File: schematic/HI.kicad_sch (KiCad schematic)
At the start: 5 parts, among them J2 USB_C_Receptacle_USB2.0, J4 Serial, SW1 Power Switch

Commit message: d
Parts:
- J2: footprint (none) -> 1KicadLib:USB4125-GF-A
- J4: footprint (none) -> Connector_PinHeader_2.54mm:PinHeader_1x03_P2.54mm_Vertical
- R8, R9: footprint (none) -> Resistor_SMD:R_0805_2012Metric_Pad1.20x1.40mm_HandSolder
- SW1: footprint (none) -> Connector_PinHeader_2.54mm:PinHeader_1x02_P2.54mm_Vertical
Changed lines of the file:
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@@
     (property "Reference" "J2" (id 0) (at 105.5878 30.0482 0))
     (property "Value" "USB_C_Receptacle_USB2.0" (id 1) (at 105.5878 32.3596 0))
-    (property "Footprint" "" (id 2) (at 106.68 52.07 0)
+    (property "Footprint" "1KicadLib:USB4125-GF-A" (id 2) (at 106.68 52.07 0)
       (effects (font (size 1.27 1.27)) hide)
     )
@@
       (effects (font (size 1.27 1.27)) (justify left))
     )
-    (property "Footprint" "" (id 2) (at 140.462 49.53 90)
+    (property "Footprint" "Resistor_SMD:R_0805_2012Metric_Pad1.20x1.40mm_HandSolder" (id 2) (at 140.462 49.53 90)
       (effects (font (size 1.27 1.27)) hide)
     )
@@
       (effects (font (size 1.27 1.27)) (justify left))
     )
-    (property "Footprint" "" (id 2) (at 148.082 46.99 90)
+    (property "Footprint" "Resistor_SMD:R_0805_2012Metric_Pad1.20x1.40mm_HandSolder" (id 2) (at 148.082 46.99 90)
       (effects (font (size 1.27 1.27)) hide)
     )
@@
     (property "Reference" "SW1" (id 0) (at 93.98 120.65 90))
     (property "Value" "Power Switch" (id 1) (at 91.44 124.46 90))
-    (property "Footprint" "" (id 2) (at 101.6 121.92 0)
+    (property "Footprint" "Connector_PinHeader_2.54mm:PinHeader_1x02_P2.54mm_Vertical" (id 2) (at 101.6 121.92 0)
       (effects (font (size 1.27 1.27)) hide)
     )
@@
       (effects (font (size 1.27 1.27)) (justify left))
     )
-    (property "Footprint" "" (id 2) (at 156.21 76.2 0)
+    (property "Footprint" "Connector_PinHeader_2.54mm:PinHeader_1x03_P2.54mm_Vertical" (id 2) (at 156.21 76.2 0)
       (effects (font (size 1.27 1.27)) hide)
     )

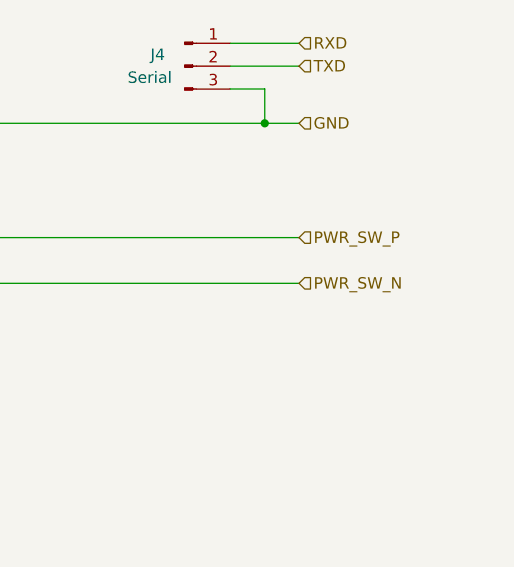
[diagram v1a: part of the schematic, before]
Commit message: beta boards routed
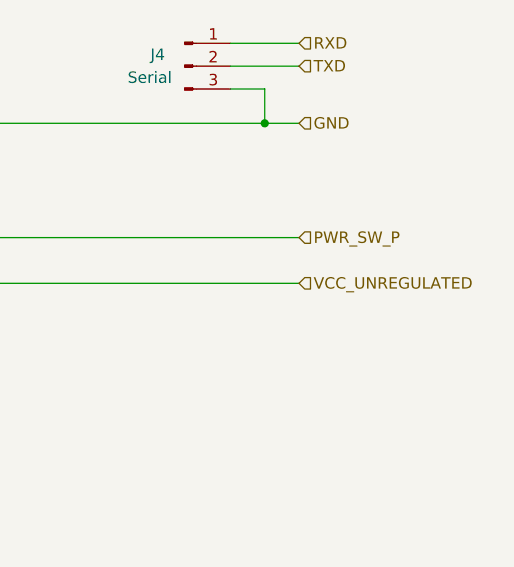
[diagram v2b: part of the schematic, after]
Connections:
- net PWR_SW_N renamed VCC_UNREGULATED
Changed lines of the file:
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@@
     (stroke (width 0) (type default) (color 0 0 0 0))
   )
-  (hierarchical_label "PWR_SW_N" (shape input) (at 168.91 100.33 0)
+  (hierarchical_label "VCC_UNREGULATED" (shape input) (at 168.91 100.33 0)
     (effects (font (size 1.27 1.27)) (justify left))
   )

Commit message: e
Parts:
- removed J4: Serial, Connector_PinHeader_2.54mm:PinHeader_1x03_P2.54mm_Vertical, symbol Connector:Conn_01x03_Male
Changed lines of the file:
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@@
   (junction (at 147.32 54.61) (diameter 0) (color 0 0 0 0)
   )
-  (junction (at 165.1 82.55) (diameter 0) (color 0 0 0 0)
-  )
   (junction (at 101.6 82.55) (diameter 0) (color 0 0 0 0)
-  )
-  (wire (pts (xy 101.6 82.55) (xy 165.1 82.55))
-    (stroke (width 0) (type default) (color 0 0 0 0))
   )
   (wire (pts (xy 101.6 114.3) (xy 101.6 107.95))
@@
   )
   (wire (pts (xy 147.32 54.61) (xy 147.32 55.88))
-    (stroke (width 0) (type default) (color 0 0 0 0))
-  )
-  (wire (pts (xy 161.29 78.74) (xy 165.1 78.74))
     (stroke (width 0) (type default) (color 0 0 0 0))
   )
@@
     (stroke (width 0) (type default) (color 0 0 0 0))
   )
-  (wire (pts (xy 168.91 66.04) (xy 163.83 66.04))
+  (wire (pts (xy 168.91 52.07) (xy 163.83 52.07))
     (stroke (width 0) (type default) (color 0 0 0 0))
   )
@@
     (stroke (width 0) (type default) (color 0 0 0 0))
   )
-  (wire (pts (xy 163.83 66.04) (xy 163.83 38.1))
+  (wire (pts (xy 163.83 52.07) (xy 163.83 38.1))
     (stroke (width 0) (type default) (color 0 0 0 0))
   )
-  (wire (pts (xy 165.1 82.55) (xy 168.91 82.55))
-    (stroke (width 0) (type default) (color 0 0 0 0))
-  )
-  (wire (pts (xy 161.29 73.66) (xy 168.91 73.66))
+  (wire (pts (xy 101.6 82.55) (xy 168.91 82.55))
     (stroke (width 0) (type default) (color 0 0 0 0))
   )
@@
     (stroke (width 0) (type default) (color 0 0 0 0))
   )
-  (wire (pts (xy 165.1 78.74) (xy 165.1 82.55))
-    (stroke (width 0) (type default) (color 0 0 0 0))
-  )
-  (wire (pts (xy 168.91 76.2) (xy 161.29 76.2))
-    (stroke (width 0) (type default) (color 0 0 0 0))
-  )
   (wire (pts (xy 93.98 82.55) (xy 93.98 76.2))
     (stroke (width 0) (type default) (color 0 0 0 0))
@@
     (effects (font (size 1.27 1.27)) (justify left))
   )
-  (hierarchical_label "RXD" (shape input) (at 168.91 73.66 0)
-    (effects (font (size 1.27 1.27)) (justify left))
-  )
   (hierarchical_label "PWR_SW_P" (shape input) (at 168.91 95.25 0)
     (effects (font (size 1.27 1.27)) (justify left))
   )
-  (hierarchical_label "VUSB" (shape input) (at 168.91 66.04 0)
+  (hierarchical_label "VUSB" (shape input) (at 168.91 52.07 0)
     (effects (font (size 1.27 1.27)) (justify left))
   )
   (hierarchical_label "GND" (shape input) (at 168.91 82.55 0)
-    (effects (font (size 1.27 1.27)) (justify left))
-  )
-  (hierarchical_label "TXD" (shape input) (at 168.91 76.2 0)
     (effects (font (size 1.27 1.27)) (justify left))
   )
@@
     (pin "2")
   )
-  (symbol (lib_id "Connector:Conn_01x03_Male") (at 156.21 76.2 0) (unit 1)
-    (in_bom yes) (on_board yes)
-    (property "Reference" "J4" (id 0) (at 152.4 74.93 0)
-      (effects (font (size 1.27 1.27)) (justify left))
-    )
-    (property "Value" "Serial" (id 1) (at 149.86 77.47 0)
-      (effects (font (size 1.27 1.27)) (justify left))
-    )
-    (property "Footprint" "Connector_PinHeader_2.54mm:PinHeader_1x03_P2.54mm_Vertical" (id 2) (at 156.21 76.2 0)
-      (effects (font (size 1.27 1.27)) hide)
-    )
-    (property "Datasheet" "~" (id 3) (at 156.21 76.2 0)
-      (effects (font (size 1.27 1.27)) hide)
-    )
-    (pin "1")
-    (pin "2")
-    (pin "3")
-  )
 )
